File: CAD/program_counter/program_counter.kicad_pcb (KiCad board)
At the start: 2 copper layers, 100 x 50 mm, 59 parts, among them J1 Conn_01x18_Pin, J2 Conn_01x06_Pin, SW1 SW_Push, SW2 SW_Push, U1 74HC161, U2 74HC161, U3 74HC161, U4 74HC161, U5 74HC245, U6 74HC245, U7 74HC165, U8 74HC165, U9 ATmega328P-A, Y1 16MHz

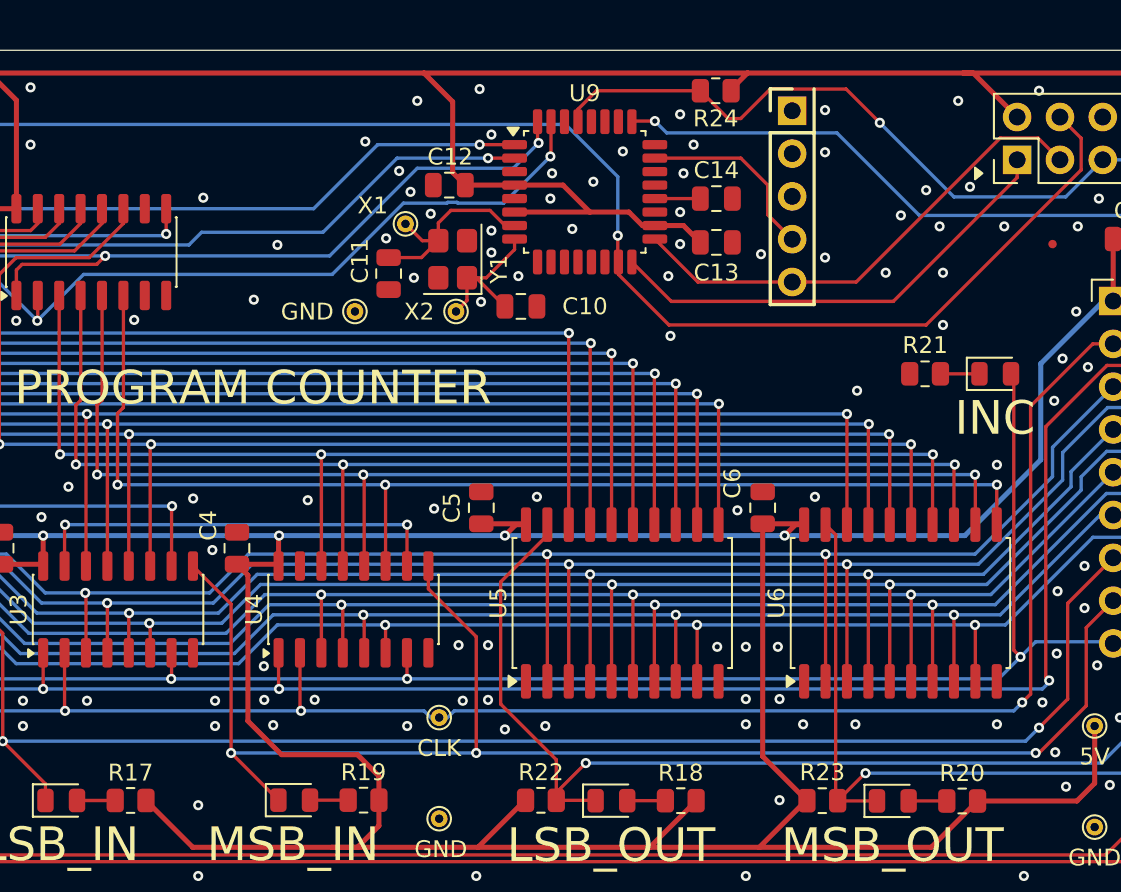
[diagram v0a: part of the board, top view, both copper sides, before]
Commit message: update KiCAD version 10.0
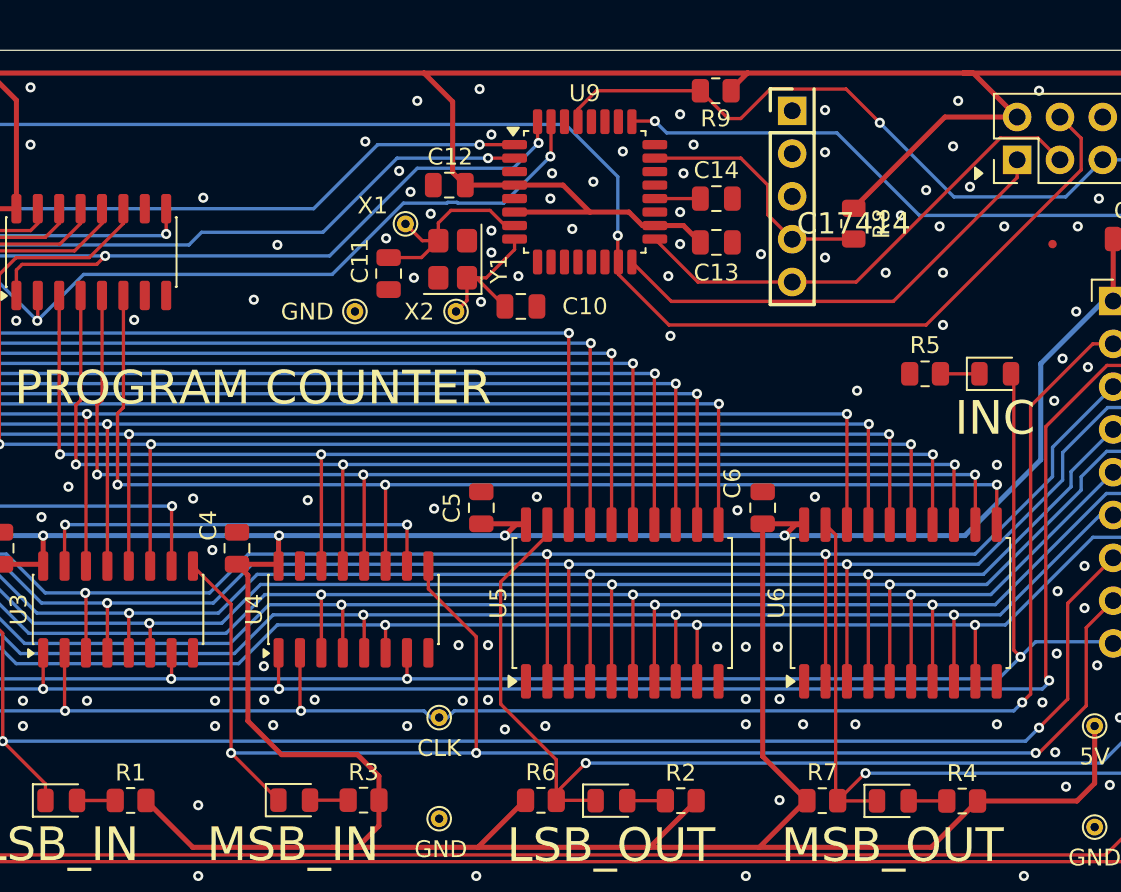
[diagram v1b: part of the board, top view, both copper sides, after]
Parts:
- removed G***: LOGO, 8-bit_computer:qr-code-github
- added R8: 10k, Resistor_SMD:R_0805_2012Metric, F.Cu at (122.7, 58.0)
- renumbered D17 to D1, D18 to D2, D19 to D3, D20 to D4, D21 to D5, R17 to R1, R18 to R2, R19 to R3, R20 to R4, R21 to R5, R22 to R6, R23 to R7, R24 to R9
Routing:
- net +5V: track 400.0 -> 412.0 mm
- net CS: track 11.2 -> 14.8 mm
- net GND: vias 153 -> 154

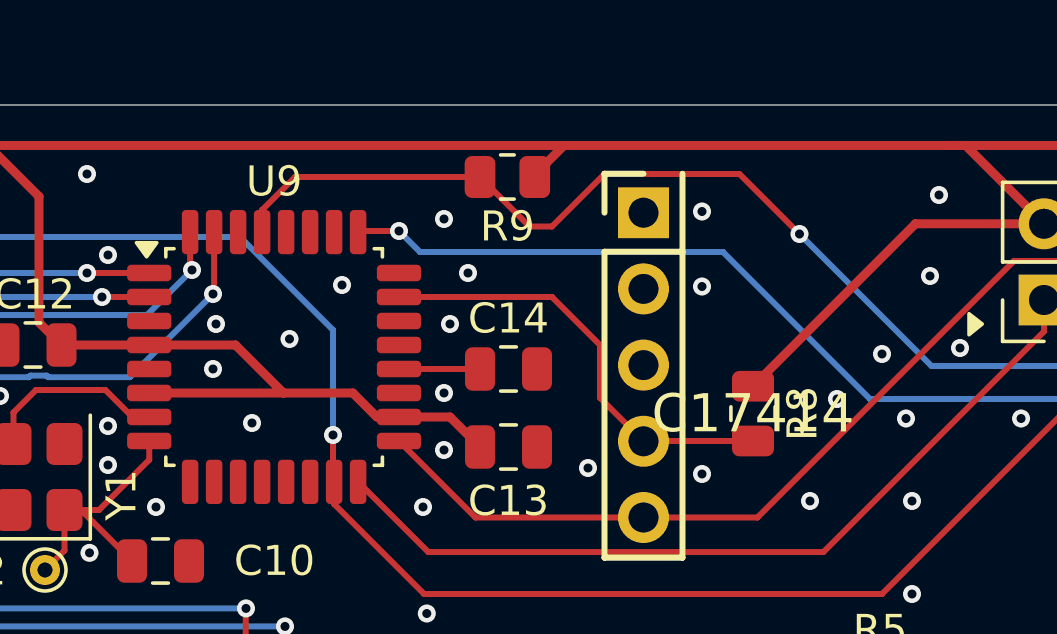
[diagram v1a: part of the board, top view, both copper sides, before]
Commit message: exclude known warnings in ERC and DRC
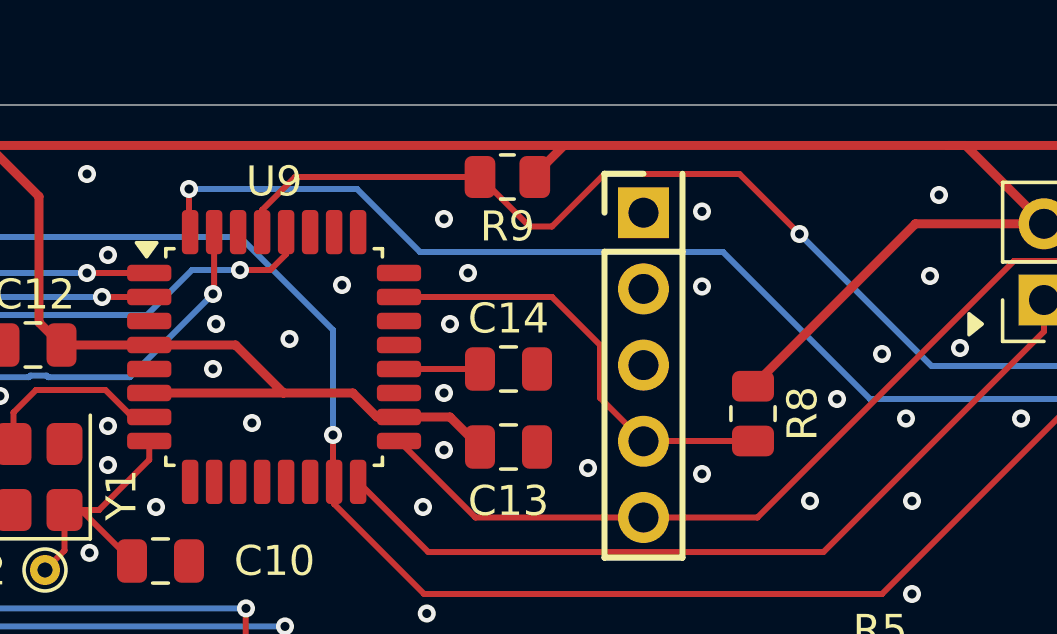
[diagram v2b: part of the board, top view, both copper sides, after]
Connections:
- U9 pad 25: ~{sw_mode} -> unconnected-(U9-PC2-Pad25)
- U9 pad 28: unconnected-(U9-PC5-Pad28) -> ~{pl}
- U9 pad 32: ~{pl} -> ~{sw_mode}
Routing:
- net ~{sw_mode}: track 151.9 -> 159.6 mm
- net ~{pl}: track 59.1 -> 61.9 mm
